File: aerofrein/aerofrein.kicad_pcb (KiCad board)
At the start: 2 copper layers, 17 parts, among them J1 endstop, J2 HMI, J3 comm, J4 power, J5 motor, J6 MS1, J7 MS2, U1 RP2040, U2 TMC2209

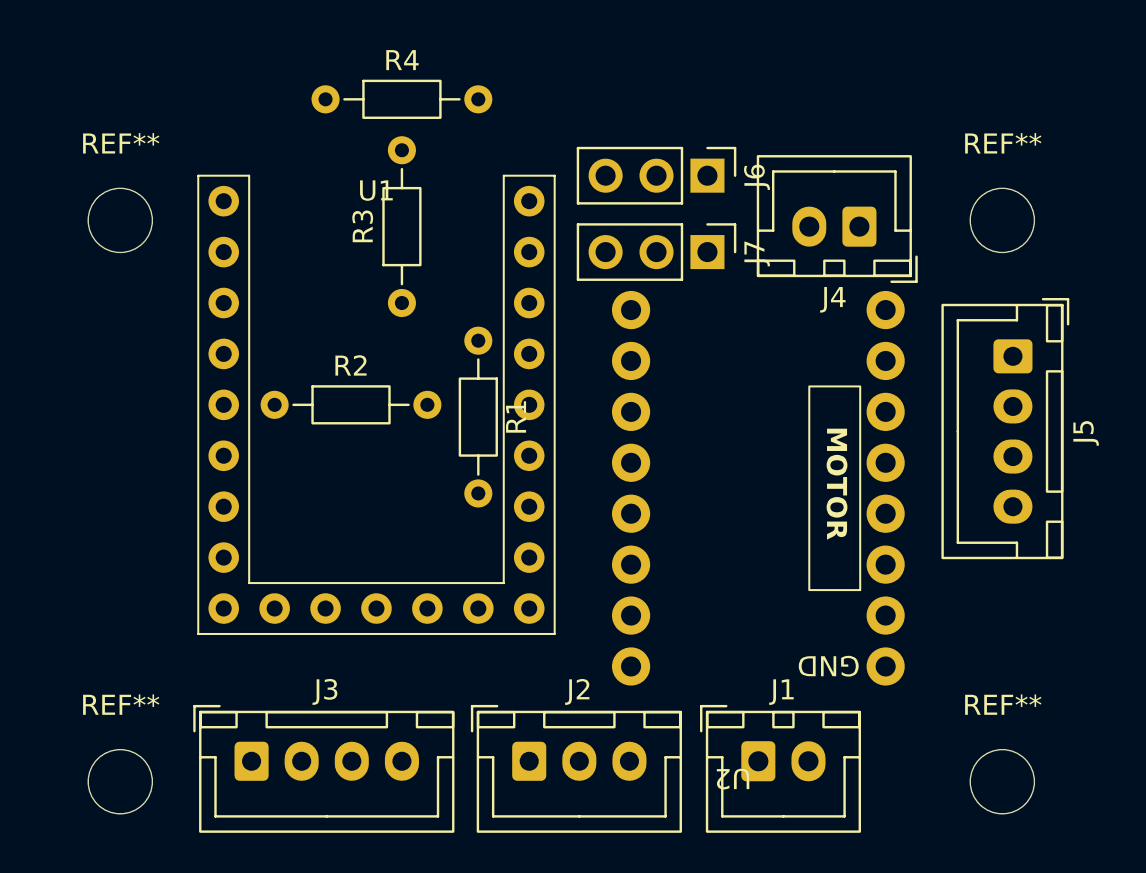
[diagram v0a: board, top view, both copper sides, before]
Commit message: création de la carte PCB aérofrein
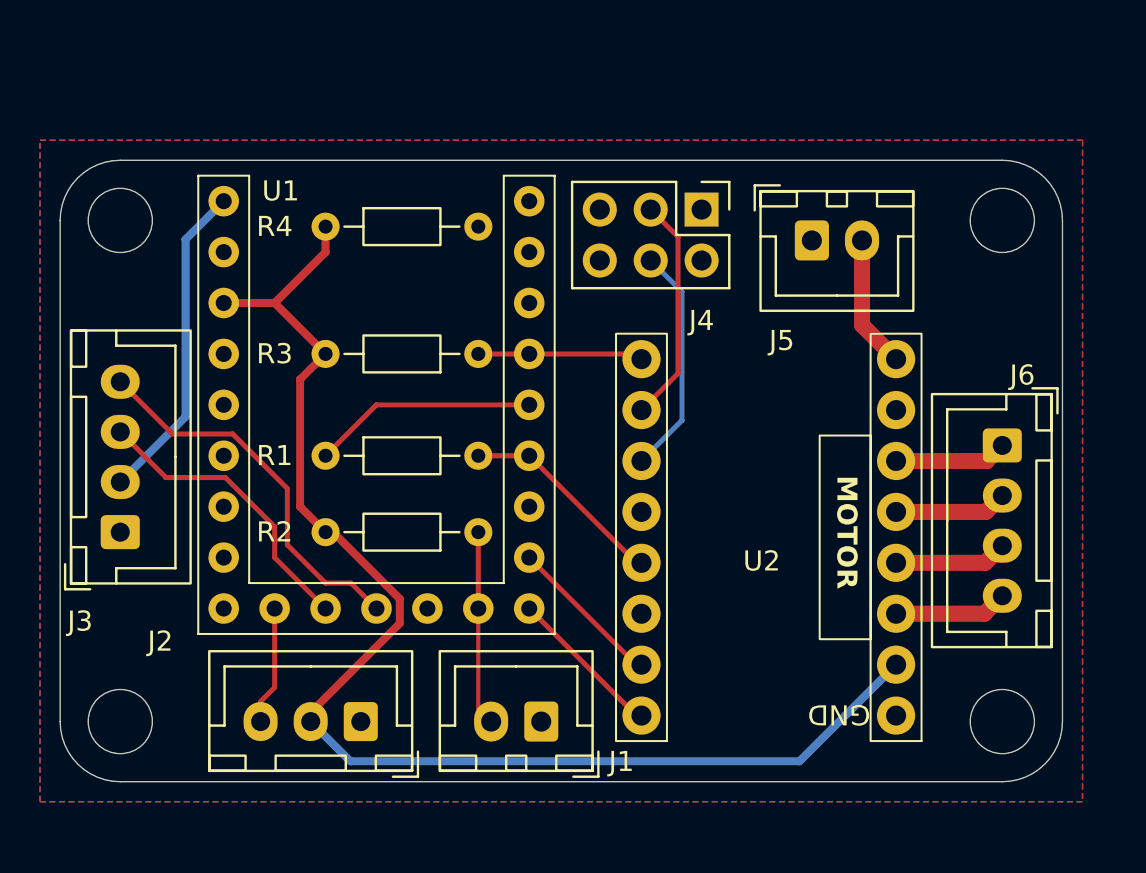
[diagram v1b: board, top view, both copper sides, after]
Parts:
- removed J7: MS2, Connector_PinHeader_2.54mm:PinHeader_1x03_P2.54mm_Vertical
- J4: value power -> MSX; footprint Connector_JST:JST_XH_B2B-XH-A_1x02_P2.50mm_Vertical -> Connector_PinHeader_2.54mm:PinHeader_2x03_P2.54mm_Vertical
- J5: value motor -> power; footprint Connector_JST:JST_XH_B4B-XH-A_1x04_P2.50mm_Vertical -> Connector_JST:JST_XH_B2B-XH-A_1x02_P2.50mm_Vertical
- J6: value MS1 -> motor; footprint Connector_PinHeader_2.54mm:PinHeader_1x03_P2.54mm_Vertical -> Connector_JST:JST_XH_B4B-XH-A_1x04_P2.50mm_Vertical
- R1, R4: value R -> 1k
- R2, R3: value R -> 10k
- moved J6 19.9 mm to (176.0, 78.2)
- moved J3 13.2 mm to (132.0, 82.5), turned to 90 degrees
- moved R2 12.0 mm to (149.9, 82.5), turned to 180 degrees
- moved J5 11.6 mm to (166.5, 68.0), turned to 0 degrees
- moved J1 11.0 mm to (153.0, 92.0), turned to 180 degrees
- moved R1 9.54 mm to (142.2, 78.7), turned to 0 degrees
- moved J2 8.63 mm to (144.0, 92.0), turned to 180 degrees
- moved J4 7.92 mm to (161.0, 66.5), turned to -90 degrees
- moved R4 6.35 mm to (142.2, 67.3)
- moved R3 4.58 mm to (149.9, 73.7), turned to 180 degrees
- moved H3 3.00 mm to (132.0, 92.0)
- moved H4 3.00 mm to (176.0, 92.0)
- moved U2 2.50 mm to (163.1, 96.8)
- renumbered REF** to H1, REF** to H2, REF** to H3, REF** to H4
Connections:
- J1 pad 2: /endstop -> /ENDSTOP
- J4 pad 2: VCC -> GND
- J5 pad 1: Net-(J5-Pin_1) -> GND
- J5 pad 2: Net-(J5-Pin_2) -> VCC
- J6 pad 1: GND -> Net-(J6-Pin_1)
- J6 pad 2: /MS1 -> Net-(J6-Pin_2)
- R2 pad 1: /endstop -> /ENDSTOP
- R4 pad 2: Net-(J6-Pin_3) -> Net-(J4-Pin_5)
- U1 pad 10: unconnected-(U1-GPIO13-Pad10) -> /LED_READY
- U1 pad 11: /LED_READY -> /SCL
- U1 pad 12: /endstop -> /SDA
- U1 pad 14: unconnected-(U1-GPIO9-Pad14) -> /ENDSTOP
- U1 pad 15: unconnected-(U1-GPIO8-Pad15) -> /TMC_DIR
- U1 pad 16: /TMC_DIR -> /TMC_STEP
- U1 pad 17: /TMC_STEP -> unconnected-(U1-GPIO6-Pad17)
- U1 pad 22: /SCL -> unconnected-(U1-GPIO1-Pad22)
- U1 pad 23: /SDA -> unconnected-(U1-GPIO0-Pad23)
- U2 pad 3: Net-(J5-Pin_4) -> Net-(J6-Pin_4)
- U2 pad 4: Net-(J5-Pin_3) -> Net-(J6-Pin_3)
- U2 pad 5: Net-(J5-Pin_2) -> Net-(J6-Pin_2)
- U2 pad 6: Net-(J5-Pin_1) -> Net-(J6-Pin_1)
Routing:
- net +3V3: track 0.00 -> 67.3 mm
- net /SDA: track 0.00 -> 19.1 mm
- net +5V: track 0.00 -> 16.1 mm
- net /SCL: track 0.00 -> 14.8 mm
- net /MS2: track 0.00 -> 11.5 mm
- net /MS1: track 0.00 -> 11.3 mm
- net Net-(U1-GPIO4): track 0.00 -> 11.2 mm
- net /TMC_IO: track 0.00 -> 10.4 mm
- net /ENDSTOP: track 0.00 -> 9.72 mm
- net /TMC_EN: track 0.00 -> 8.25 mm
- net /TMC_STEP: track 0.00 -> 7.81 mm
- net /TMC_DIR: track 0.00 -> 7.81 mm
- net VCC: track 0.00 -> 6.63 mm
- net /LED_READY: track 0.00 -> 5.93 mm
- net Net-(J6-Pin_4): track 0.00 -> 5.67 mm
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- added copper zone on B.Cu, net GND
- added copper zone on F.Cu, net GND
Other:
- board outline added: 50 x 31 mm
- board text added: "0"
- board text added: "1"
- board text added: "10k"
- board text added: "1k"
- board text added: "HMI"
- board text added: "MOTOR"
- board text added: "MS1"
- board text added: "MS2"
- board text added: "Vcc motor"
- board text added: "comm"
- board text added: "endstop"

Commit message: correction PCB
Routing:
- net Net-(J4-Pin_5): track 0.00 -> 8.80 mm
- net +3V3: track 67.3 -> 66.0 mm
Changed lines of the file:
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@@
-	)
-	(segment
-		(start 138.43 71.12)
-		(end 137.16 71.12)
-		(width 0.4)
-		(layer "F.Cu")
-		(net 7)
 	)
 	(segment
@@
 	)
 	(segment
+		(start 139.7 71.12)
+		(end 142.24 73.66)
+		(width 0.4)
+		(layer "F.Cu")
+		(net 7)
+	)
+	(segment
+		(start 141.5 91.545)
+		(end 141.5 92)
+		(width 0.4)
+		(layer "F.Cu")
+		(net 7)
+	)
+	(segment
+		(start 140.97 74.93)
+		(end 142.24 73.66)
+		(width 0.4)
+		(layer "F.Cu")
+		(net 7)
+	)
+	(segment
+		(start 140.97 81.28)
+		(end 140.97 74.93)
+		(width 0.4)
+		(layer "F.Cu")
+		(net 7)
+	)
+	(segment
+		(start 142.24 67.31)
+		(end 142.24 68.58)
+		(width 0.4)
+		(layer "F.Cu")
+		(net 7)
+	)
+	(segment
 		(start 137.16 71.12)
 		(end 139.7 71.12)
@@
 	)
 	(segment
-		(start 139.7 71.12)
-		(end 142.24 73.66)
-		(width 0.4)
-		(layer "F.Cu")
-		(net 7)
-	)
-	(segment
-		(start 141.5 91.545)
-		(end 141.5 92)
-		(width 0.4)
-		(layer "F.Cu")
-		(net 7)
-	)
-	(segment
-		(start 140.97 74.93)
-		(end 142.24 73.66)
-		(width 0.4)
-		(layer "F.Cu")
-		(net 7)
-	)
-	(segment
-		(start 140.97 81.28)
-		(end 140.97 74.93)
-		(width 0.4)
-		(layer "F.Cu")
-		(net 7)
-	)
-	(segment
-		(start 142.24 67.31)
-		(end 142.24 68.58)
-		(width 0.4)
-		(layer "F.Cu")
-		(net 7)
-	)
-	(segment
 		(start 142.24 82.55)
 		(end 142.614731 82.55)
@@
 	(segment
 		(start 132 80.05)
-		(end 135.255 76.795)
+		(end 135.89 76.16)
 		(width 0.4)
 		(layer "B.Cu")
@@
 	)
 	(segment
-		(start 135.255 76.795)
-		(end 135.255 67.945)
+		(start 135.89 76.16)
+		(end 135.89 67.31)
 		(width 0.4)
 		(layer "B.Cu")
@@
 	)
 	(segment
-		(start 135.255 67.945)
+		(start 135.89 67.31)
 		(end 137.16 66.04)
 		(width 0.4)
@@
 		(net 32)
 	)
+	(segment
+		(start 155.92 66.46)
+		(end 155.07 67.31)
+		(width 0.25)
+		(layer "F.Cu")
+		(net 33)
+	)
+	(segment
+		(start 154.23 67.31)
+		(end 155.92 69)
+		(width 0.25)
+		(layer "F.Cu")
+		(net 33)
+	)
+	(segment
+		(start 149.86 67.31)
+		(end 154.23 67.31)
+		(width 0.25)
+		(layer "F.Cu")
+		(net 33)
+	)
+	(segment
+		(start 155.07 67.31)
+		(end 154.23 67.31)
+		(width 0.25)
+		(layer "F.Cu")
+		(net 33)
+	)
 	(zone

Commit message: airbrake full revision
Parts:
- removed H2, H3, H4: MountingHole_3.2mm_M3_ISO7380, MountingHole:MountingHole_3.2mm_M3_ISO7380
- added H1: MountingHole_3.2mm_M3_ISO7380, MountingHole:MountingHole_3.2mm_M3_ISO7380, F.Cu at (132.0, 93.0)
- added H1: MountingHole_3.2mm_M3_ISO7380, MountingHole:MountingHole_3.2mm_M3_ISO7380, F.Cu at (176.0, 93.0)
- added H1: MountingHole_3.2mm_M3_ISO7380, MountingHole:MountingHole_3.2mm_M3_ISO7380, F.Cu at (176.0, 68.0)
- moved H1 1.00 mm to (132.0, 68.0)
- moved J4 0.90 mm to (161.3, 67.3)
- moved U1 0.90 mm to (145.4, 66.7)
- moved J2 0.76 mm to (144.3, 92.7)
- moved J1 0.71 mm to (153.0, 92.7)
- moved U2 0.64 mm to (162.6, 97.2)
- moved R1 0.64 mm to (142.2, 79.4)
- moved R2 0.64 mm to (149.9, 83.2)
- moved R3 0.64 mm to (149.9, 74.3)
- moved R4 0.63 mm to (142.2, 67.9)
- moved J5 0.40 mm to (166.4, 68.4)
- moved J3 0.38 mm to (132.1, 82.9)
- moved J6 0.10 mm to (175.9, 78.2)
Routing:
- net +3V3: track 66.0 -> 61.5 mm
- net +5V: track 16.1 -> 19.0 mm
- net /MS2: track 11.5 -> 10.4 mm
- net /SCL: track 14.8 -> 15.8 mm
- net /SDA: track 19.1 -> 20.1 mm
- net /TMC_STEP: track 7.81 -> 6.92 mm
- net /TMC_DIR: track 7.81 -> 6.92 mm
- net Net-(U1-GPIO4): track 11.2 -> 11.8 mm
- net /TMC_EN: track 8.25 -> 7.62 mm
- net Net-(J6-Pin_4): track 5.67 -> 6.24 mm
- net Net-(J6-Pin_2): track 5.64 -> 6.21 mm
- net Net-(J6-Pin_1): track 5.62 -> 6.19 mm
- net Net-(J6-Pin_3): track 5.65 -> 6.22 mm
